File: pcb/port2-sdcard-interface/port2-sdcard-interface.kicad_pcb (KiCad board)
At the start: 4 copper layers, 80 x 100 mm, 58 parts, among them J2 P2000T Port 2, J3 SD Card, U1 CY62128ELL-45SXI, U10 74HC32, U11 74HC273, U12 74HC165, U13 74HC595, U14 74HC00, U15 SST39SF010, U17 74HC138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

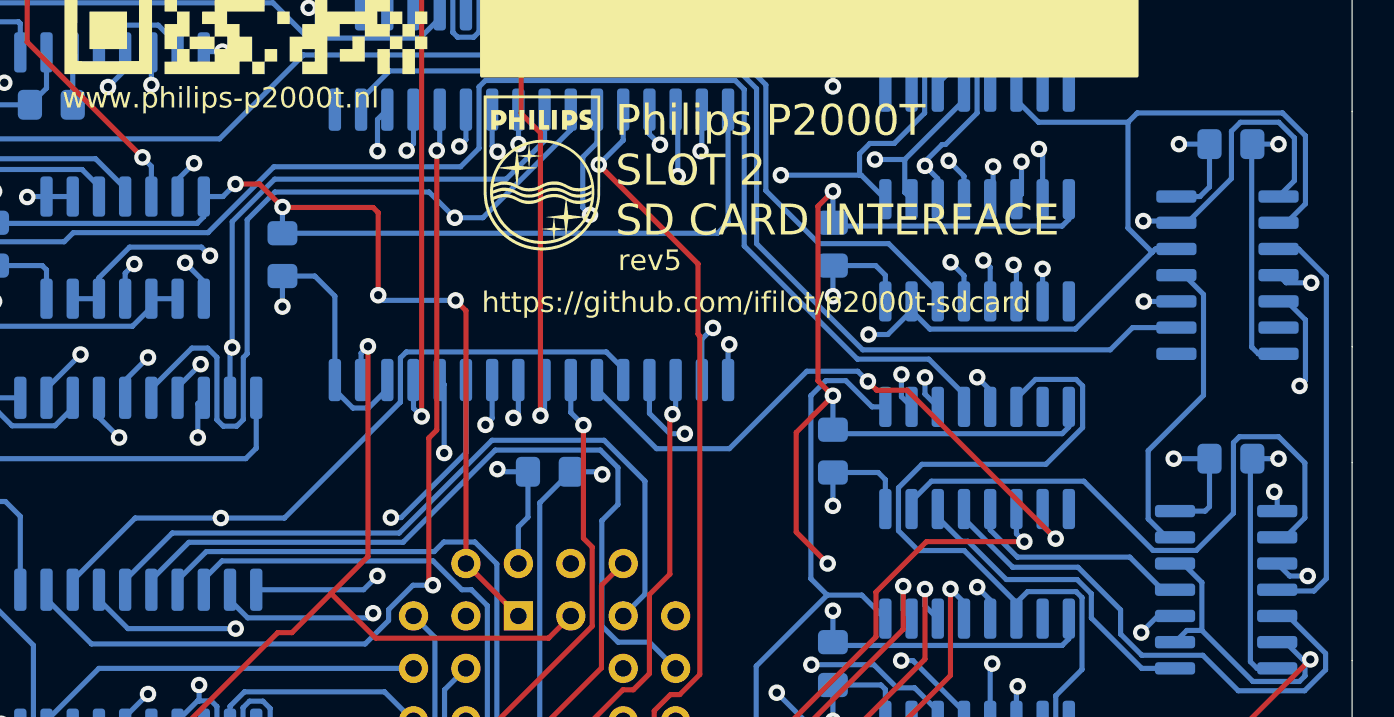
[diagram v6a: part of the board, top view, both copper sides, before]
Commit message: Patch v0.6.0 (#7)
* Adding memory model

* Allowing execution of custom programs from SD card

* Removing wrong files

* Further pruning obsolete files

* Replacing front images

* Expanding README.md

* Revising image

* Allowing launching of external programs

* Showing partition size and removing less relevant data

* Fixing typos

* Adding hexdumps for ROM, RAM and main memory

* Expanding README.md

* Adding CRC16 check for monitor and shuffling routines

* Pruning map file

* Adding routine to test for the presence of an SD-card

* Compiling programs

* Signing

* Packaging programs

* Listing files

* Fixing

* Fix unique name issue

* Attempt 2

* Different zipping

* Fixing signing

* Expanding README.md file

* Adding OSHW logo
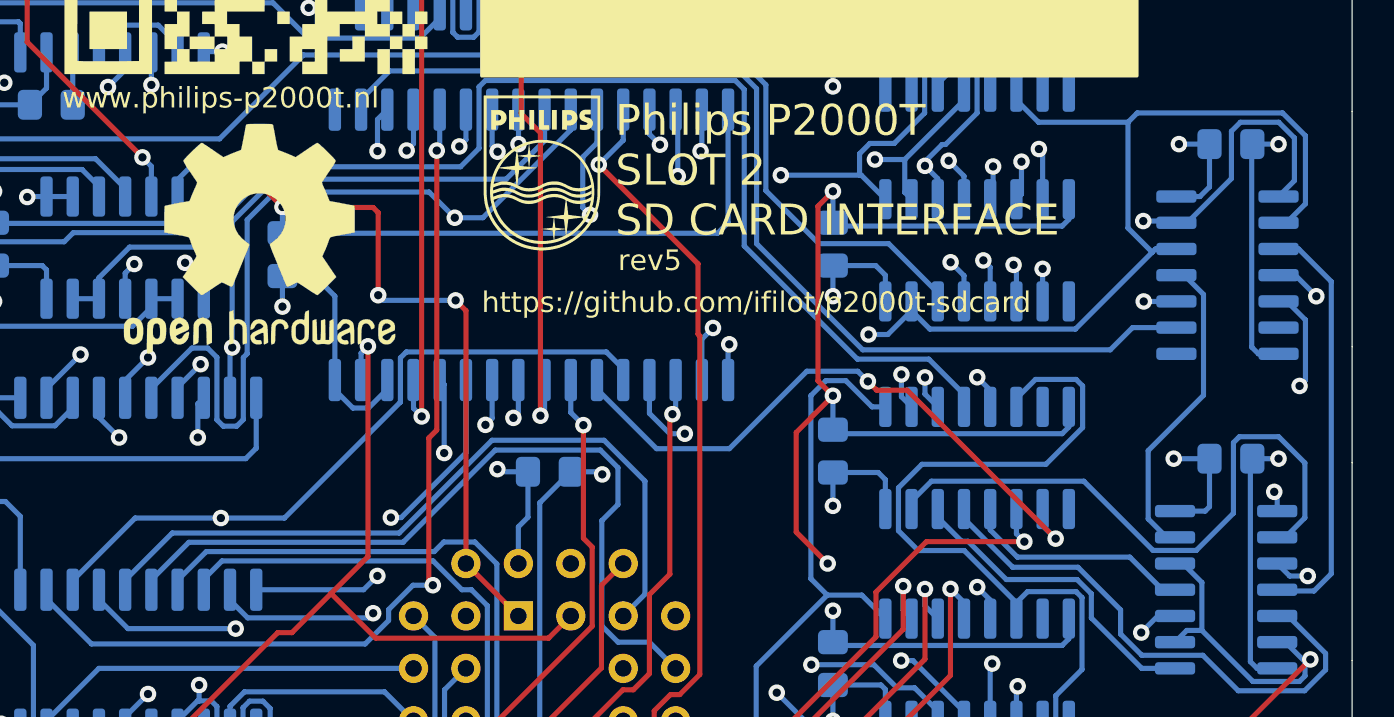
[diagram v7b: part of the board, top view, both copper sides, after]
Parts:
- added REF**: OSHW-Logo2_14.6x12mm_SilkScreen, Symbol:OSHW-Logo2_14.6x12mm_SilkScreen, F.Cu at (48.7, 63.2)
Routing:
- net VCC: track 193.7 -> 194.3 mm
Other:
- board text added: "(bank)"
- board text added: "(led)"

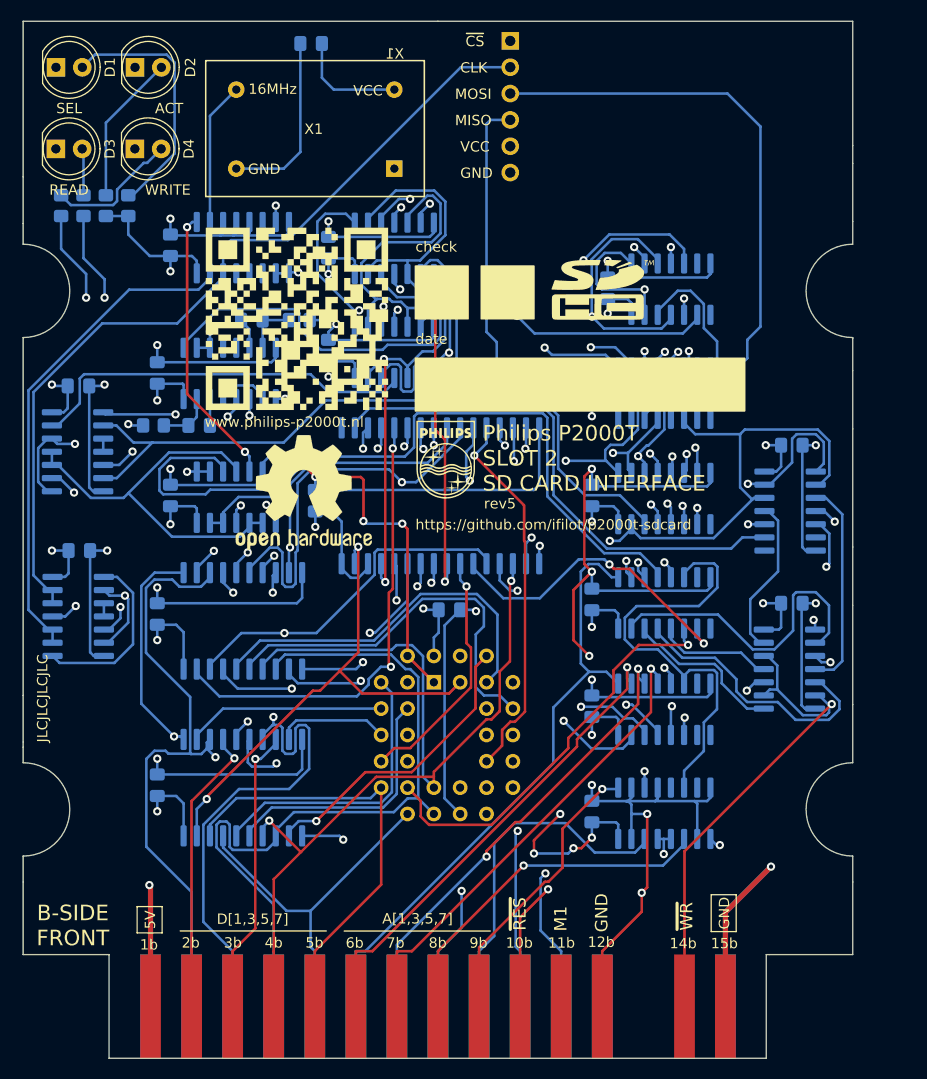
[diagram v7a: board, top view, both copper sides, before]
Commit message: PCB revision 6 (#9)
* Setting port addresses in header and include files

* Updating rev and changing 0x60 to 0x40

* Changing port for BASICmod

* Incrementing version number

* Adding enclosure files, changing CI and adding option to disable hardware test

* Fixing CI

* Adding README.md
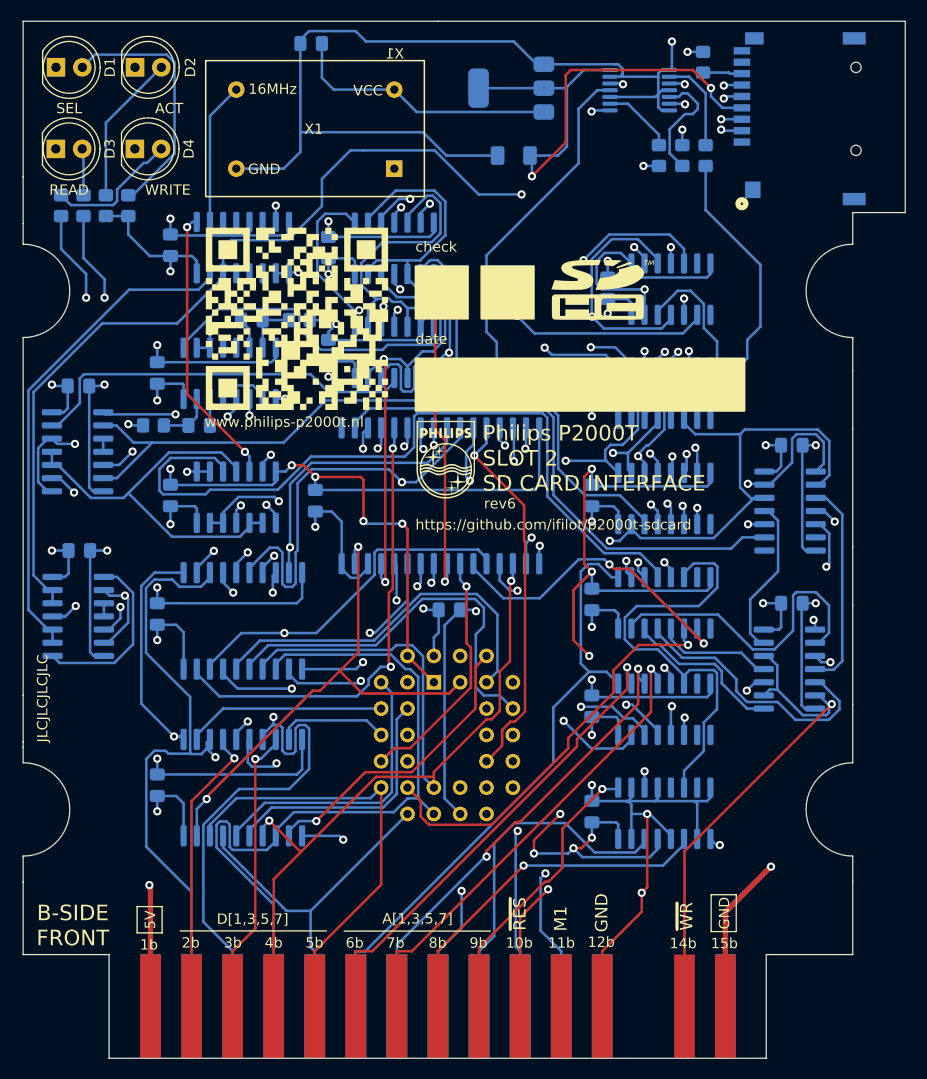
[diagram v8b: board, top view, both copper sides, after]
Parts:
- removed J3: SD Card, Connector_PinSocket_2.54mm:PinSocket_1x06_P2.54mm_Vertical
- removed REF**: OSHW-Logo2_14.6x12mm_SilkScreen, Symbol:OSHW-Logo2_14.6x12mm_SilkScreen
- added C23: 100nF, Capacitor_SMD:C_1206_3216Metric_Pad1.33x1.80mm_HandSolder, B.Cu at (68.9, 30.7)
- added J1: Micro_SD_Card_Det1, components:CONN9_MSD-1_CUD, B.Cu at (98.7, 27.2)
- added R10: 3.3k, Resistor_SMD:R_0805_2012Metric_Pad1.20x1.40mm_HandSolder, B.Cu at (85.2, 30.7)
- added R11: 3.3k, Resistor_SMD:R_0805_2012Metric_Pad1.20x1.40mm_HandSolder, B.Cu at (82.9, 30.7)
- added R8: 3.3k, Resistor_SMD:R_0805_2012Metric_Pad1.20x1.40mm_HandSolder, B.Cu at (87.2, 21.7)
- added R9: 3.3k, Resistor_SMD:R_0805_2012Metric_Pad1.20x1.40mm_HandSolder, B.Cu at (87.4, 30.7)
- added U16: AMS1117-3.3, Package_TO_SOT_SMD:SOT-223-3_TabPin2, B.Cu at (68.7, 24.2)
- added U21: 74LVC125, Package_SO:TSSOP-14_4.4x5mm_P0.65mm, B.Cu at (81.0, 24.4)
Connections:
- U20 pad 12: VCC -> GND
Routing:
- net GND: track 448.9 -> 528.3 mm, vias 27 -> 29
- net +3V3: track 0.00 -> 56.3 mm, vias 0 -> 2
- net MOSI: track 55.6 -> 28.6 mm
- net ~{CS}: track 77.3 -> 101.0 mm, vias 1 -> 2
- net VCC: track 194.3 -> 216.7 mm, vias 37 -> 36
- net CS_LLS: track 0.00 -> 17.1 mm, vias 0 -> 2
- net Net-(R10-Pad2): track 0.00 -> 11.4 mm
- net Net-(R8-Pad2): track 0.00 -> 10.3 mm, vias 0 -> 2
- net Net-(R9-Pad2): track 0.00 -> 9.16 mm
- net DI_LLS: track 0.00 -> 8.43 mm, vias 0 -> 2
- net SCK_LLS: track 0.00 -> 7.34 mm, vias 0 -> 2
- net CLK: track 133.2 -> 140.5 mm, vias 1 -> 3
- net Net-(R11-Pad2): track 0.00 -> 6.97 mm
- net MISO: track 51.0 -> 57.4 mm
- net D0_LLS: track 0.00 -> 3.79 mm
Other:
- board size 80 x 100 mm -> 85.1 x 100 mm
- board text added: "3.3k"
- board text added: "rev6"
- board text removed: "rev5"
- board text removed: "~{CS}"
